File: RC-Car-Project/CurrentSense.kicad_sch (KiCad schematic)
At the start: 0 parts

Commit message: Add libraries and components in schs
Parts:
- added U8: INA229AQDGSRQ1, VSSOP10_DGS_TEX, symbol INA229AQDGSRQ1:INA229AQDGSRQ1
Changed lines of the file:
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@@
 	(generator_version "8.0")
 	(paper "A4")
+	(symbol
+		(lib_id "INA229AQDGSRQ1:INA229AQDGSRQ1")
+		(at 113.03 86.36 0)
+		(unit 1)
+		(exclude_from_sim no)
+		(in_bom yes)
+		(on_board yes)
+		(dnp no)
+		(fields_autoplaced yes)
+		(property "Reference" "U8"
+			(at 133.35 76.2 0)
+			(effects
+				(font
+					(size 1.524 1.524)
+				)
+			)
+		)
+		(property "Value" "INA229AQDGSRQ1"
+			(at 133.35 78.74 0)
+			(effects
+				(font
+					(size 1.524 1.524)
+				)
+			)
+		)
+		(property "Footprint" "VSSOP10_DGS_TEX"
+			(at 113.03 86.36 0)
+			(effects
+				(font
+					(size 1.27 1.27)
+					(italic yes)
+				)
+				(hide yes)
+			)
+		)
+		(property "Datasheet" "INA229AQDGSRQ1"
+			(at 113.03 86.36 0)
+			(effects
+				(font
+					(size 1.27 1.27)
+					(italic yes)
+				)
+				(hide yes)
+			)
+		)
+		(property "Description" ""
+			(at 113.03 86.36 0)
+			(effects
+				(font
+					(size 1.27 1.27)
+				)
+				(hide yes)
+			)
+		)
+		(pin "9"
+		)
+		(pin "5"
+		)
+		(pin "1"
+		)
+		(pin "8"
+		)
+		(pin "10"
+		)
+		(pin "2"
+		)
+		(pin "7"
+		)
+		(pin "4"
+		)
+		(pin "6"
+		)
+		(pin "3"
+		)
+		(instances
+			(project ""
+				(path "/ba870fd1-751d-4755-8e1a-1ea86ca9e2f6/9035ce50-cc35-47ce-85b3-06db8b07dac9"
+					(reference "U8")
+					(unit 1)
+				)
+			)
+		)
+	)
 )

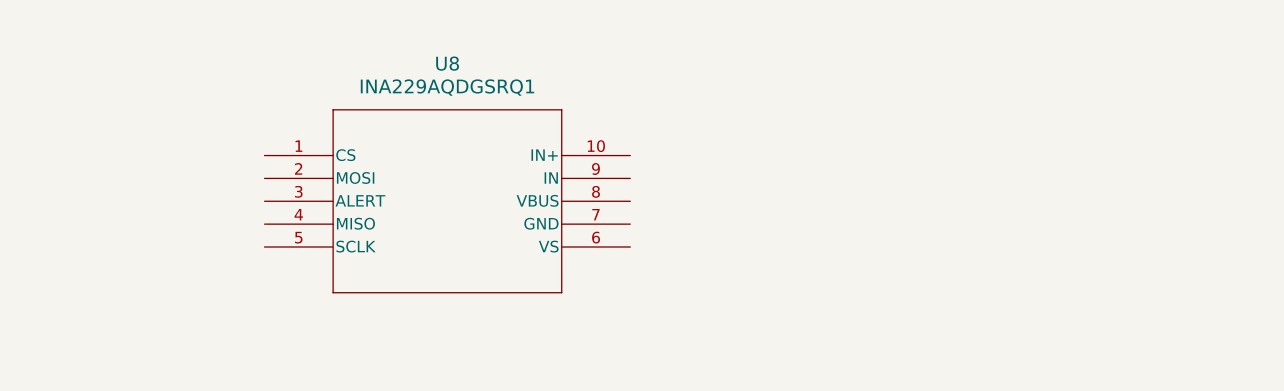
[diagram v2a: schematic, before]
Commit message: Added Basic Schematic + STM32 Project config. TODO: Component value selection + double check all connections.
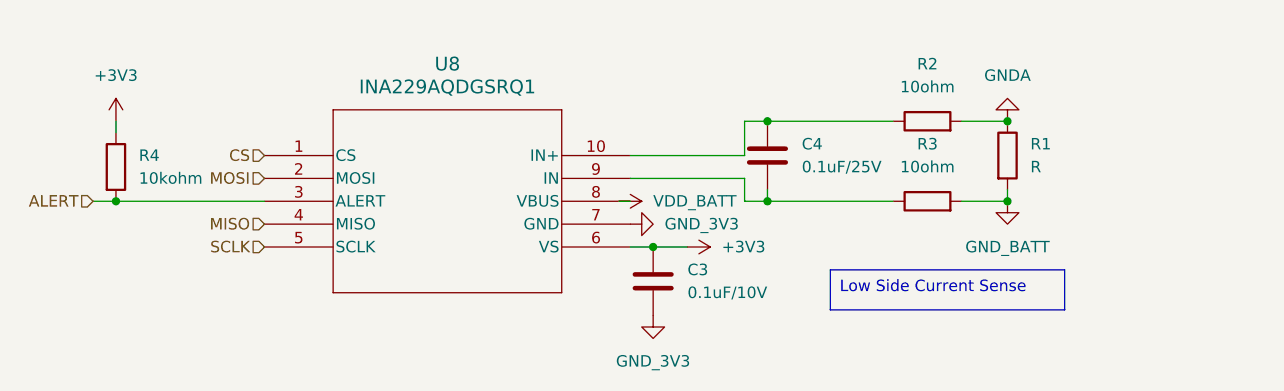
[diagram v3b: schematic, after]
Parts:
- added C3: 0.1uF/10V, symbol Device:C
- added C4: 0.1uF/25V, symbol Device:C
- added R1: R, symbol Device:R
- added R2, R3: 10ohm, symbol Device:R
- added R4: 10kohm, symbol Device:R
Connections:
- net CS: now reaches U8.1 (CS)
- net at U8.10 (IN+): now also C4.1, R2.1
- net MOSI: now reaches U8.2 (MOSI)
- net ALERT: now reaches U8.3 (ALERT)
- net ALERT: now also R4.2
- net MISO: now reaches U8.4 (MISO)
- net SCLK: now reaches U8.5 (SCLK)
- net +3V3: now reaches U8.6 (VS)
- net +3V3: now also C3.1, R4.1
- net GND_3V3: now reaches U8.7 (GND)
- net GND_3V3: now also C3.2
- net VDD_BATT: now reaches U8.8 (VBUS)
- net at U8.9 (IN): now also C4.2, R3.1
- new net GNDA: R1.1, R2.2
- new net GND_BATT: R1.2, R3.2

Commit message: Connector stuff
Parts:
- removed R1: R, symbol Device:R
- added R15: WSL27262L000FEB, WSL2726_VIS, symbol WSL27262L000FEB:WSL27262L000FEB
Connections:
- net GNDA: now also R15.1; no longer R2.2
- net GND_BATT: now also R15.4; no longer R3.2
- new net: R15.2, R2.2
- new net: R15.3, R3.2
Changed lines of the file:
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@@
-	)
-	(junction
-		(at 195.58 82.55)
-		(diameter 0)
-		(color 0 0 0 0)
 	)
 	(junction
@@
 	(junction
 		(at 96.52 91.44)
-		(diameter 0)
-		(color 0 0 0 0)
-	)
-	(junction
-		(at 195.58 91.44)
 		(diameter 0)
 		(color 0 0 0 0)
@@
 	(text_box "Low Side Current Sense\n"
 		(exclude_from_sim no)
-		(at 175.895 99.06 0)
+		(at 175.895 103.505 0)
 		(size 26.035 4.445)
 		(stroke
@@
 	)
 	(symbol
-		(lib_id "Device:R")
-		(at 195.58 86.36 0)
-		(unit 1)
-		(exclude_from_sim no)
-		(in_bom yes)
-		(on_board yes)
-		(dnp no)
-		(fields_autoplaced yes)
-		(property "Reference" "R1"
-			(at 198.12 85.0899 0)
-			(effects
-				(font
-					(size 1.27 1.27)
-				)
-				(justify left)
-			)
-		)
-		(property "Value" "R"
-			(at 198.12 87.6299 0)
-			(effects
-				(font
-					(size 1.27 1.27)
-				)
-				(justify left)
-			)
-		)
-		(property "Footprint" ""
-			(at 193.802 86.36 90)
-			(effects
-				(font
-					(size 1.27 1.27)
-				)
-				(hide yes)
-			)
-		)
-		(property "Datasheet" "~"
-			(at 195.58 86.36 0)
-			(effects
-				(font
-					(size 1.27 1.27)
-				)
-				(hide yes)
-			)
-		)
-		(property "Description" "Resistor"
-			(at 195.58 86.36 0)
-			(effects
-				(font
-					(size 1.27 1.27)
-				)
-				(hide yes)
-			)
-		)
-		(pin "1"
-		)
-		(pin "2"
-		)
-		(instances
-			(project ""
-				(path "/ba870fd1-751d-4755-8e1a-1ea86ca9e2f6/9035ce50-cc35-47ce-85b3-06db8b07dac9"
-					(reference "R1")
-					(unit 1)
-				)
-			)
-		)
-	)
-	(symbol
 		(lib_id "power:GNDA")
-		(at 195.58 82.55 180)
+		(at 195.58 77.47 180)
 		(unit 1)
 		(exclude_from_sim no)
@@
 		(fields_autoplaced yes)
 		(property "Reference" "#PWR020"
-			(at 195.58 76.2 0)
+			(at 195.58 71.12 0)
 			(effects
 				(font
@@
 		)
 		(property "Value" "GNDA"
+			(at 195.58 72.39 0)
+			(effects
+				(font
+					(size 1.27 1.27)
+				)
+			)
+		)
+		(property "Footprint" ""
 			(at 195.58 77.47 0)
 			(effects
@@
 					(size 1.27 1.27)
 				)
-			)
-		)
-		(property "Footprint" ""
-			(at 195.58 82.55 0)
-			(effects
-				(font
-					(size 1.27 1.27)
-				)
 				(hide yes)
 			)
 		)
 		(property "Datasheet" ""
-			(at 195.58 82.55 0)
+			(at 195.58 77.47 0)
 			(effects
 				(font
@@
 		)
 		(property "Description" "Power symbol creates a global label with name \"GNDA\" , analog ground"
-			(at 195.58 82.55 0)
+			(at 195.58 77.47 0)
 			(effects
 				(font
@@
 				(path "/ba870fd1-751d-4755-8e1a-1ea86ca9e2f6/9035ce50-cc35-47ce-85b3-06db8b07dac9"
 					(reference "#PWR020")
+					(unit 1)
+				)
+			)
+		)
+	)
+	(symbol
+		(lib_id "WSL27262L000FEB:WSL27262L000FEB")
+		(at 195.58 80.01 270)
+		(unit 1)
+		(exclude_from_sim no)
+		(in_bom yes)
+		(on_board yes)
+		(dnp no)
+		(fields_autoplaced yes)
+		(property "Reference" "R15"
+			(at 200.66 85.0899 90)
+			(effects
+				(font
+					(size 1.524 1.524)
+				)
+				(justify left)
+			)
+		)
+		(property "Value" "WSL27262L000FEB"
+			(at 200.66 87.6299 90)
+			(effects
+				(font
+					(size 1.524 1.524)
+				)
+				(justify left)
+			)
+		)
+		(property "Footprint" "WSL2726_VIS"
+			(at 195.58 80.01 0)
+			(effects
+				(font
+					(size 1.27 1.27)
+					(italic yes)
+				)
+				(hide yes)
+			)
+		)
+		(property "Datasheet" "WSL27262L000FEB"
+			(at 195.58 80.01 0)
+			(effects
+				(font
+					(size 1.27 1.27)
+					(italic yes)
+				)
+				(hide yes)
+			)
+		)
+		(property "Description" ""
+			(at 195.58 80.01 0)
+			(effects
+				(font
+					(size 1.27 1.27)
+				)
+				(hide yes)
+			)
+		)
+		(pin "2"
+		)
+		(pin "1"
+		)
+		(pin "3"
+		)
+		(pin "4"
+		)
+		(instances
+			(project ""
+				(path "/ba870fd1-751d-4755-8e1a-1ea86ca9e2f6/9035ce50-cc35-47ce-85b3-06db8b07dac9"
+					(reference "R15")
 					(unit 1)
 				)
@@
 	)
 	(symbol
-		(lib_id "power:GND")
-		(at 195.58 91.44 0)
-		(unit 1)
-		(exclude_from_sim no)
-		(in_bom yes)
-		(on_board yes)
-		(dnp no)
-		(fields_autoplaced yes)
-		(property "Reference" "#PWR021"
-			(at 195.58 97.79 0)
-			(effects
-				(font
-					(size 1.27 1.27)
-				)
-				(hide yes)
-			)
-		)
-		(property "Value" "GND_BATT"
-			(at 195.58 96.52 0)
-			(effects
-				(font
-					(size 1.27 1.27)
-				)
-			)
-		)
-		(property "Footprint" ""
-			(at 195.58 91.44 0)
-			(effects
-				(font
-					(size 1.27 1.27)
-				)
-				(hide yes)
-			)
-		)
-		(property "Datasheet" ""
-			(at 195.58 91.44 0)
-			(effects
-				(font
-					(size 1.27 1.27)
-				)
-				(hide yes)
-			)
-		)
-		(property "Description" "Power symbol creates a global label with name \"GND\" , ground"
-			(at 195.58 91.44 0)
-			(effects
-				(font
-					(size 1.27 1.27)
-				)
-				(hide yes)
-			)
-		)
-		(pin "1"
-		)
-		(instances
-			(project "RC-Car-Project"
-				(path "/ba870fd1-751d-4755-8e1a-1ea86ca9e2f6/9035ce50-cc35-47ce-85b3-06db8b07dac9"
-					(reference "#PWR021")
-					(unit 1)
-				)
-			)
-		)
-	)
-	(symbol
 		(lib_id "Device:C")
 		(at 168.91 86.36 0)
@@
 					(unit 1)
 				)
+			)
+		)
+	)
+	(symbol
+		(lib_id "power:GND")
+		(at 195.58 95.25 0)
+		(unit 1)
+		(exclude_from_sim no)
+		(in_bom yes)
+		(on_board yes)
+		(dnp no)
+		(fields_autoplaced yes)
+		(property "Reference" "#PWR087"
+			(at 195.58 101.6 0)
+			(effects
+				(font
+					(size 1.27 1.27)
+				)
+				(hide yes)
+			)
+		)
+		(property "Value" "GND_BATT"
+			(at 195.58 100.33 0)
+			(effects
+				(font
+					(size 1.27 1.27)
+				)
+			)
+		)
+		(property "Footprint" ""
+			(at 195.58 95.25 0)
+			(effects
+				(font
+					(size 1.27 1.27)
+				)
+				(hide yes)
+			)
+		)
+		(property "Datasheet" ""
+			(at 195.58 95.25 0)
+			(effects
+				(font
+					(size 1.27 1.27)
+				)
+				(hide yes)
+			)
+		)
+		(property "Description" "Power symbol creates a global label with name \"GND\" , ground"
+			(at 195.58 95.25 0)
+			(effects
+				(font
+					(size 1.27 1.27)
+				)
+				(hide yes)
+			)
+		)
+		(pin "1"
+		)
+		(instances
+			(project "RC-Car-Project"
+				(path "/ba870fd1-751d-4755-8e1a-1ea86ca9e2f6/9035ce50-cc35-47ce-85b3-06db8b07dac9"
+					(reference "#PWR087")
+					(unit 1)
+				)
